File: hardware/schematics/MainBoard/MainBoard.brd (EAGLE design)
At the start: 85.1 x 107.6 mm, 17 parts

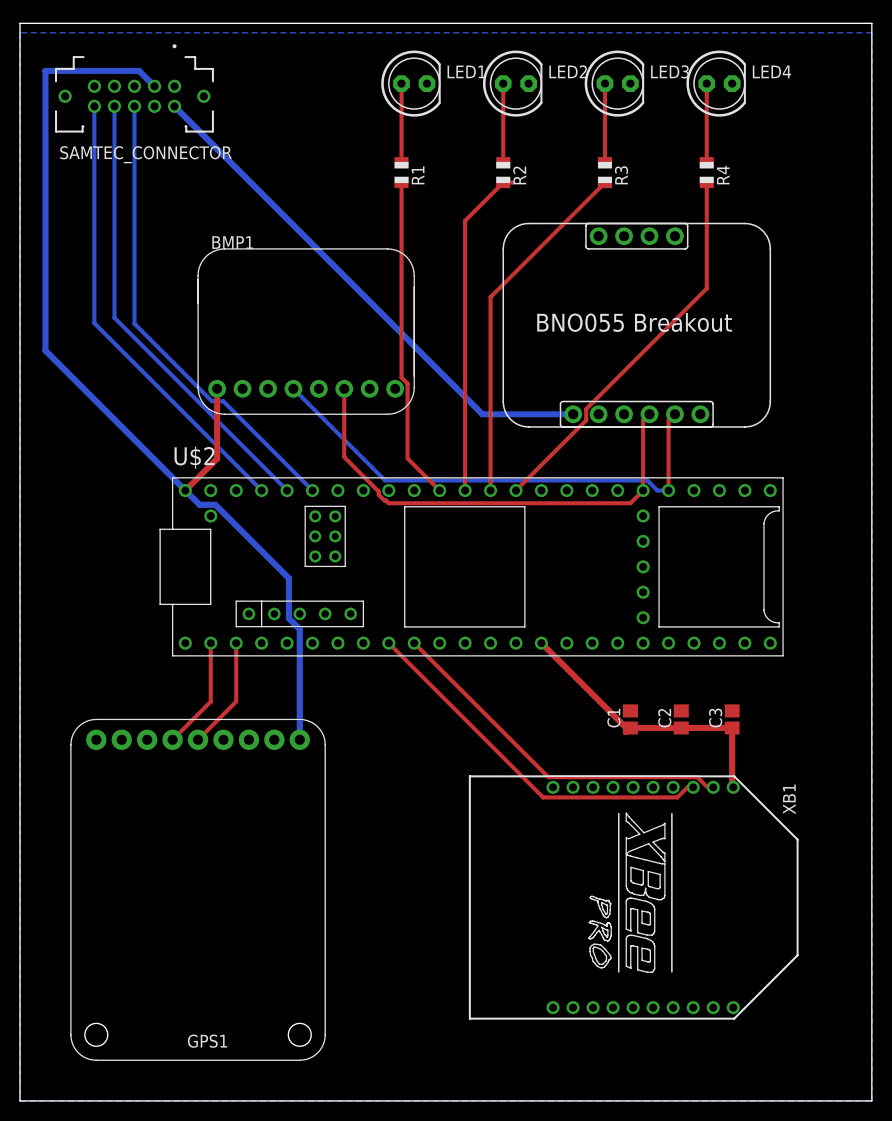
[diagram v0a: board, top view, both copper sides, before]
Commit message: Updates
Made power traces wider
Added XBEE enable and reset traces
Moved I2C pins to correct pins on teensy
Made caps 805 size
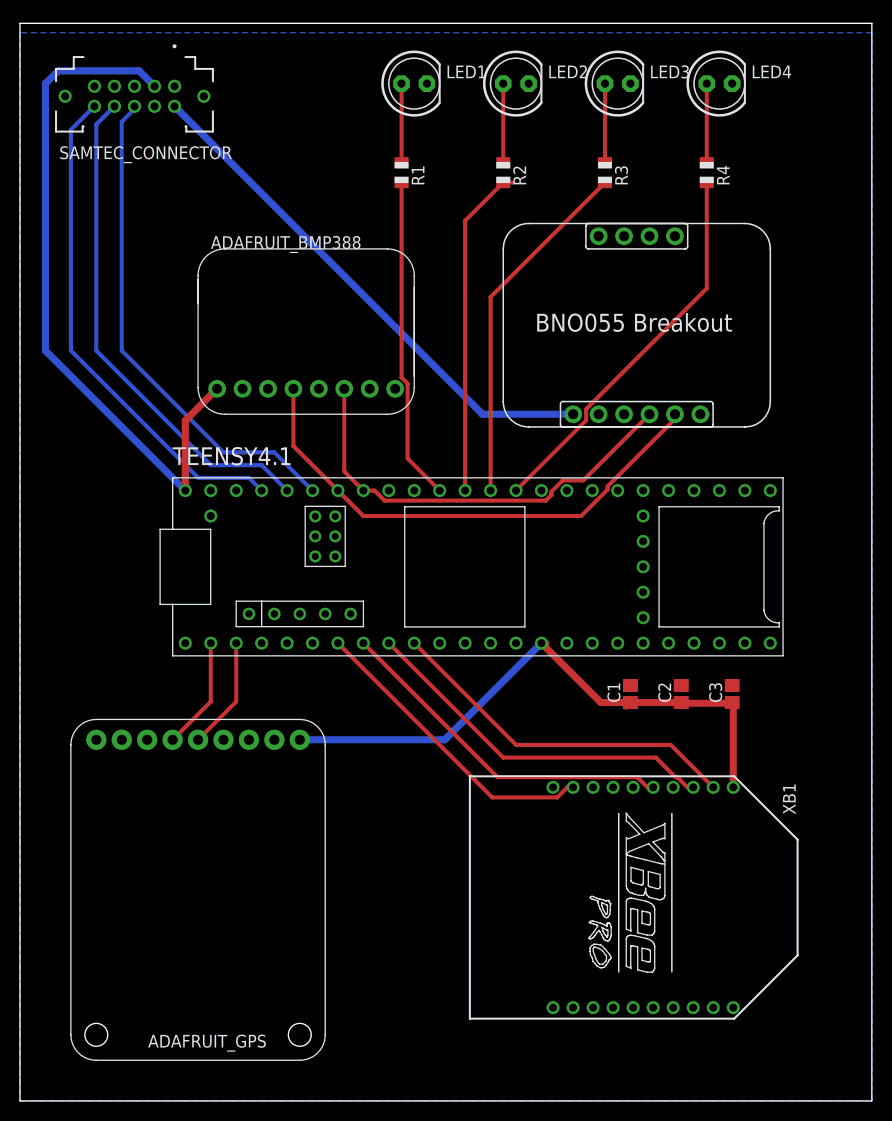
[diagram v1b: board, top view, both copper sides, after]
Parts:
- moved C1 2.54 mm to (61.0, 40.6)
- moved C2 2.54 mm to (66.0, 40.6)
- moved C3 2.54 mm to (71.1, 40.6)
- renumbered BMP1 to ADAFRUIT_BMP388, GPS1 to ADAFRUIT_GPS, U$2 to TEENSY4.1
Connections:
- net SCL: now also TEENSY4.1.D20/A6; no longer TEENSY4.1.D37
- net SDA: now also TEENSY4.1.D19/A5; no longer TEENSY4.1.D38/A14
- net XBEE_EN: now also TEENSY4.1.D5
- net XBEE_RST: now also TEENSY4.1.D6
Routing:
- net XBEE_RST: track 0.00 -> 34.9 mm
- net XBEE_EN: track 0.00 -> 30.3 mm
- net V_BATT: track 45.3 -> 50.2 mm
- net I_SENSE: track 45.5 -> 50.0 mm
- net SDA: track 47.2 -> 43.7 mm
- net BATT_TEMP: track 46.4 -> 49.8 mm
- net SCL: track 49.6 -> 51.4 mm
- net XBEE_TX: track 37.2 -> 36.4 mm

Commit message: Added top layer ground pour
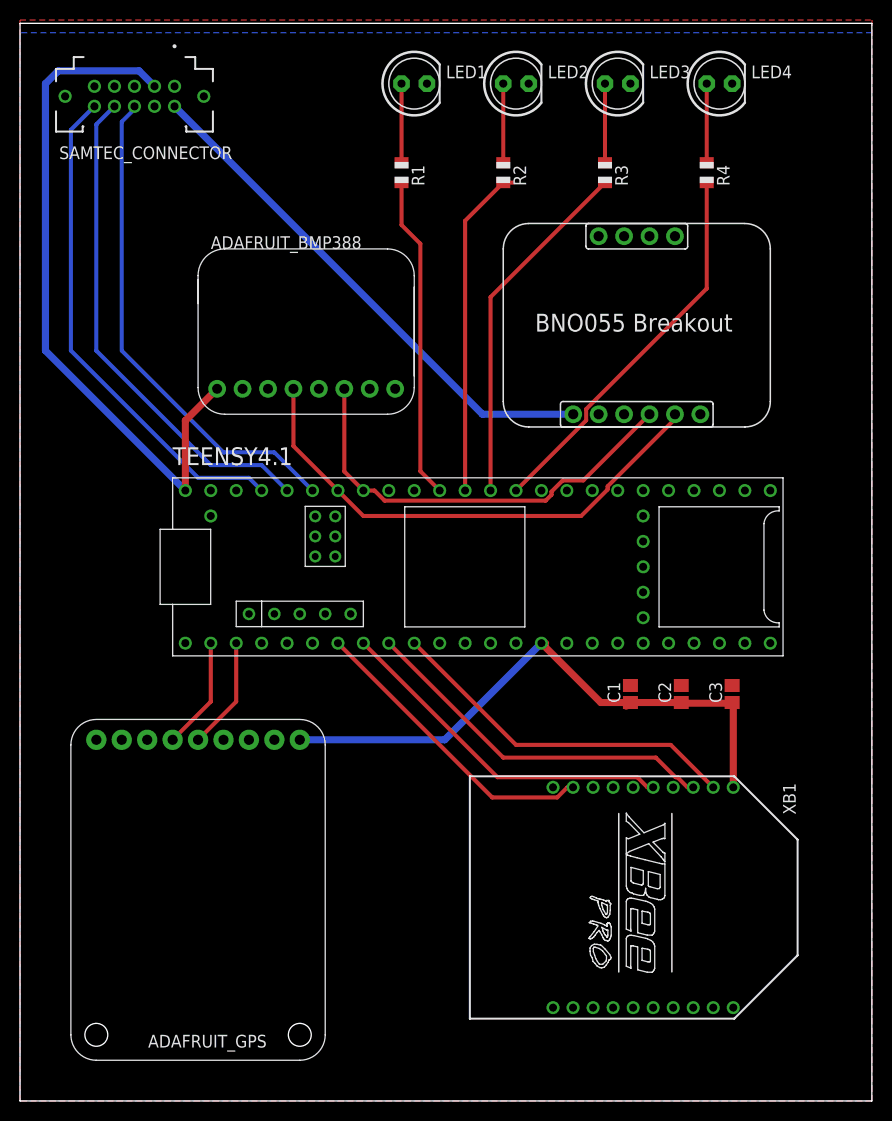
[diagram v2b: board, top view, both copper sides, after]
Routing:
- added copper zone on layer 1, net GND
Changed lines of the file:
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@@
 </polygon>
 <contactref element="ADAFRUIT_BMP388" pad="GND"/>
-<wire x1="66.04" y1="41.49" x2="71.12" y2="41.49" width="0" layer="19" extent="1-1"/>
-<wire x1="60.96" y1="41.49" x2="66.04" y2="41.49" width="0" layer="19" extent="1-1"/>
-<wire x1="62.23" y1="53.34" x2="60.96" y2="41.49" width="0" layer="19" extent="1-1"/>
+<polygon width="0.1524" layer="1" isolate="0.4064">
+<vertex x="0" y="107.95"/>
+<vertex x="85.09" y="107.95"/>
+<vertex x="85.09" y="0"/>
+<vertex x="0" y="0"/>
+</polygon>
 </signal>
 <signal name="AGND">
@@
 <contactref element="R1" pad="2"/>
 <contactref element="TEENSY4.1" pad="D16/A2"/>
-<wire x1="38.7096" y1="71.63553125" x2="38.1" y2="72.24513125" width="0.4064" layer="1"/>
-<wire x1="38.1" y1="72.24513125" x2="38.1" y2="91.71" width="0.4064" layer="1"/>
-<wire x1="41.91" y1="60.96" x2="38.7096" y2="64.1604" width="0.4064" layer="1"/>
-<wire x1="38.7096" y1="64.1604" x2="38.7096" y2="71.63553125" width="0.4064" layer="1"/>
+<wire x1="39.9796" y1="85.60553125" x2="38.1" y2="87.48513125" width="0.4064" layer="1"/>
+<wire x1="38.1" y1="87.48513125" x2="38.1" y2="91.71" width="0.4064" layer="1"/>
+<wire x1="41.91" y1="60.96" x2="39.9796" y2="62.8904" width="0.4064" layer="1"/>
+<wire x1="39.9796" y1="62.8904" x2="39.9796" y2="85.60553125" width="0.4064" layer="1"/>
 </signal>
 <signal name="LED_2">

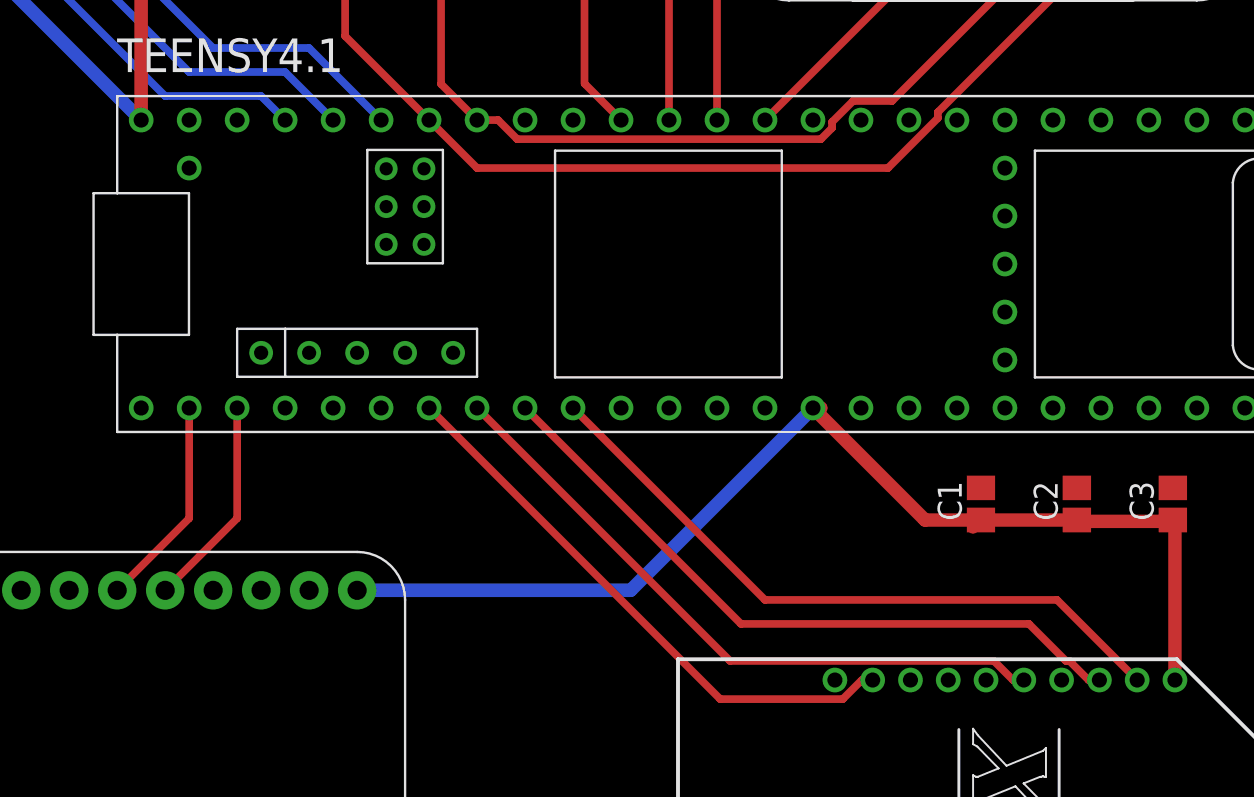
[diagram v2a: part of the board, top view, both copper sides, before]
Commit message: Fixed TX/RX pins for GPS and Xbee
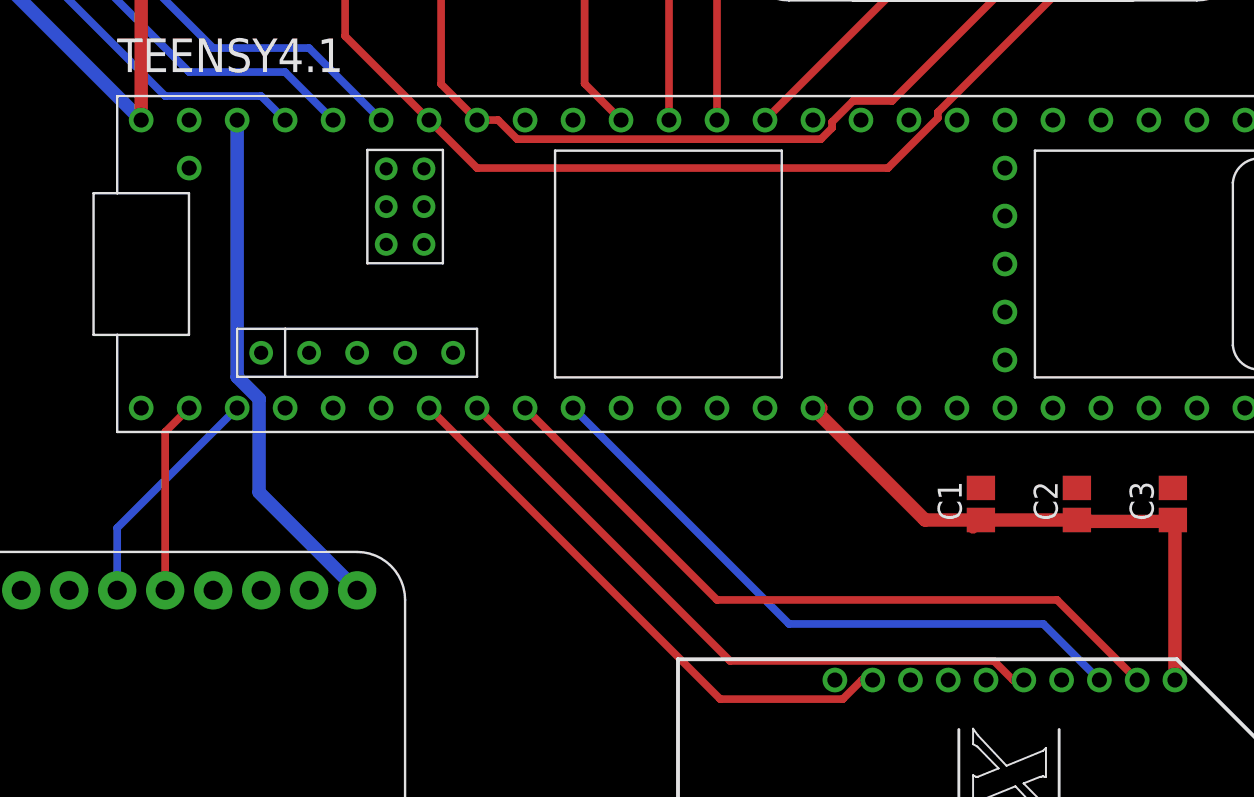
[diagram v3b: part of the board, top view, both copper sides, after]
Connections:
- net 3.3V: no longer TEENSY4.1.3.3V@1
- net 3V3: now also TEENSY4.1.3.3V@1
- net GPS_RX: now also TEENSY4.1.D1; no longer TEENSY4.1.D0
- net GPS_TX: now also TEENSY4.1.D0; no longer TEENSY4.1.D1
- net XBEE_RX: now also XB1.3; no longer XB1.2
- net XBEE_TX: now also XB1.2; no longer XB1.3
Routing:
- net XBEE_TX: track 36.4 -> 38.4 mm
- net XBEE_RX: track 35.8 -> 33.8 mm
- net GPS_RX: track 11.2 -> 12.3 mm
- net GPS_TX: track 11.2 -> 10.2 mm
- net 3V3: track 130.2 -> 129.6 mm
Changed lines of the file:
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@@
 <drawing>
 <settings>
-<setting alwaysvectorfont="yes"/>
+<setting alwaysvectorfont="no"/>
 <setting verticaltext="up"/>
 </settings>
@@
 <signal name="3.3V">
 <contactref element="TEENSY4.1" pad="3.3V@2"/>
-<contactref element="TEENSY4.1" pad="3.3V@1"/>
-<wire x1="21.59" y1="60.96" x2="62.23" y2="50.8" width="0" layer="19" extent="1-1"/>
 </signal>
 <signal name="VBAT">
@@
 <wire x1="60.96" y1="39.79" x2="58" y2="39.79" width="0.7112" layer="1"/>
 <wire x1="58" y1="39.79" x2="52.07" y2="45.72" width="0.7112" layer="1"/>
-<wire x1="27.94" y1="36.068" x2="42.418" y2="36.068" width="0.7112" layer="16"/>
-<wire x1="42.418" y1="36.068" x2="52.07" y2="45.72" width="0.7112" layer="16"/>
 <wire x1="16.51" y1="60.96" x2="16.51" y2="67.945" width="0.7112" layer="1"/>
 <wire x1="16.51" y1="67.945" x2="19.685" y2="71.12" width="0.7112" layer="1"/>
@@
 <wire x1="11.89" y1="102.87" x2="13.43" y2="101.33" width="0.7112" layer="16"/>
 <wire x1="3.81" y1="102.87" x2="11.89" y2="102.87" width="0.7112" layer="16"/>
-<wire x1="27.94" y1="36.068" x2="16.51" y2="60.96" width="0" layer="19" extent="1-1"/>
+<contactref element="TEENSY4.1" pad="3.3V@1"/>
+<wire x1="21.59" y1="47.36331875" x2="21.59" y2="60.96" width="0.7112" layer="16"/>
+<wire x1="22.752" y1="46.20131875" x2="21.59" y2="47.36331875" width="0.7112" layer="16"/>
+<wire x1="27.94" y1="36.068" x2="22.752" y2="41.256" width="0.7112" layer="16"/>
+<wire x1="22.752" y1="41.256" x2="22.752" y2="46.20131875" width="0.7112" layer="16"/>
+<wire x1="27.94" y1="36.068" x2="52.07" y2="45.72" width="0" layer="19" extent="1-1"/>
+<wire x1="16.51" y1="60.96" x2="21.59" y2="60.96" width="0" layer="19" extent="1-1"/>
 </signal>
 <signal name="GPS_TX">
 <contactref element="ADAFRUIT_GPS" pad="TX"/>
-<contactref element="TEENSY4.1" pad="D1"/>
-<wire x1="21.59" y1="45.72" x2="21.59" y2="39.878" width="0.4064" layer="1"/>
-<wire x1="17.78" y1="36.068" x2="21.59" y2="39.878" width="0.4064" layer="1"/>
+<contactref element="TEENSY4.1" pad="D0"/>
+<wire x1="17.78" y1="36.068" x2="17.78" y2="44.45" width="0.4064" layer="1"/>
+<wire x1="17.78" y1="44.45" x2="19.05" y2="45.72" width="0.4064" layer="1"/>
 </signal>
 <signal name="GPS_RX">
 <contactref element="ADAFRUIT_GPS" pad="RX"/>
-<contactref element="TEENSY4.1" pad="D0"/>
-<wire x1="19.05" y1="45.72" x2="19.05" y2="39.878" width="0.4064" layer="1"/>
-<wire x1="15.24" y1="36.068" x2="19.05" y2="39.878" width="0.4064" layer="1"/>
+<contactref element="TEENSY4.1" pad="D1"/>
+<wire x1="15.24" y1="36.068" x2="15.24" y2="39.37" width="0.4064" layer="16"/>
+<wire x1="15.24" y1="39.37" x2="21.59" y2="45.72" width="0.4064" layer="16"/>
 </signal>
 <signal name="XBEE_TX">
-<contactref element="XB1" pad="3"/>
 <contactref element="TEENSY4.1" pad="D7"/>
-<wire x1="48.26" y1="34.29" x2="36.83" y2="45.72" width="0.4064" layer="1"/>
-<wire x1="65.64819375" y1="32.3296" x2="65.4604" y2="32.3296" width="0.4064" layer="1"/>
-<wire x1="65.4604" y1="32.3296" x2="63.5" y2="34.29" width="0.4064" layer="1"/>
-<wire x1="67.23" y1="31.32" x2="66.65779375" y2="31.32" width="0.4064" layer="1"/>
-<wire x1="66.65779375" y1="31.32" x2="65.64819375" y2="32.3296" width="0.4064" layer="1"/>
-<wire x1="63.5" y1="34.29" x2="48.26" y2="34.29" width="0.4064" layer="1"/>
+<contactref element="XB1" pad="2"/>
+<wire x1="46.99" y1="35.56" x2="36.83" y2="45.72" width="0.4064" layer="1"/>
+<wire x1="69.23" y1="31.32" x2="64.99" y2="35.56" width="0.4064" layer="1"/>
+<wire x1="64.99" y1="35.56" x2="46.99" y2="35.56" width="0.4064" layer="1"/>
 </signal>
 <signal name="XBEE_RST">
@@
 <signal name="XBEE_RX">
 <contactref element="TEENSY4.1" pad="D8"/>
-<contactref element="XB1" pad="2"/>
-<wire x1="39.37" y1="45.72" x2="49.53" y2="35.56" width="0.4064" layer="1"/>
-<wire x1="64.99" y1="35.56" x2="69.23" y2="31.32" width="0.4064" layer="1"/>
-<wire x1="49.53" y1="35.56" x2="64.99" y2="35.56" width="0.4064" layer="1"/>
+<contactref element="XB1" pad="3"/>
+<wire x1="39.37" y1="45.72" x2="50.8" y2="34.29" width="0.4064" layer="16"/>
+<wire x1="64.26" y1="34.29" x2="67.23" y2="31.32" width="0.4064" layer="16"/>
+<wire x1="50.8" y1="34.29" x2="64.26" y2="34.29" width="0.4064" layer="16"/>
 </signal>
 <signal name="XBEE_EN">
